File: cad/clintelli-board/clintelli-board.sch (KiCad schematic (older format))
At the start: 26 parts, among them IC1 ATMEGA328-A, P1 CONN_01X16, P2 CONN_01X14, P3 CONN_01X14, P4 CONN_01X01, P5 CONN_01X01, P6 CONN_01X01, SW1 SW_PUSH, U1 3v3, U2 ESP8266EX, U3 ADS1298xPAG, U4 ATECC608A-MAHDA, Y1 16M

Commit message: Schematic changes: - Replaced ESP8266 with ESP32 - Added AudioJack connector - Removed Header pins
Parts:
- removed P1: CONN_01X16, Pin_Headers:Pin_Header_Straight_1x16_Pitch2.54mm, symbol clintelli-board-rescue:CONN_01X16-Pyramiduino-rescue
- removed P2: CONN_01X14, Pin_Headers:Pin_Header_Straight_1x15_Pitch2.54mm, symbol clintelli-board-rescue:CONN_01X15-Pyramiduino-rescue
- removed P3: CONN_01X14, Pin_Headers:Pin_Header_Straight_1x14_Pitch2.54mm, symbol clintelli-board-rescue:CONN_01X14-Pyramiduino-rescue
- removed U2: ESP8266EX, Package_DFN_QFN:QFN-32-1EP_5x5mm_P0.5mm_EP3.45x3.45mm, symbol MCU_Espressif:ESP8266EX
- added J1: AudioJack3_Ground, symbol Connector:AudioJack3_Ground
- added U2: ESP32-WROOM-32, RF_Module:ESP32-WROOM-32, symbol RF_Module:ESP32-WROOM-32
- C1, C2, C3, C4, C5, C6, C7, C8, C9: symbol clintelli-board-rescue:C-Pyramiduino-rescue -> clintelli-board-rescue:C
- D1: symbol clintelli-board-rescue:LED-Pyramiduino-rescue -> clintelli-board-rescue:LED
- IC1: symbol clintelli-board-rescue:ATMEGA328-A-Pyramiduino-rescue -> clintelli-board-rescue:ATMEGA328-A
- L1: symbol clintelli-board-rescue:INDUCTOR-Pyramiduino-rescue -> clintelli-board-rescue:INDUCTOR
- P4, P5, P6: symbol clintelli-board-rescue:CONN_01X01-Pyramiduino-rescue -> clintelli-board-rescue:CONN_01X01
- R1, R2: symbol clintelli-board-rescue:R-Pyramiduino-rescue -> clintelli-board-rescue:R
- SW1: symbol clintelli-board-rescue:SW_PUSH-Pyramiduino-rescue -> clintelli-board-rescue:SW_PUSH
- U1: symbol clintelli-board-rescue:MIC5504-3.3YM5-Pyramiduino-rescue -> clintelli-board-rescue:MIC5504-3.3YM5
- Y1: symbol clintelli-board-rescue:Crystal_GND24-Pyramiduino-rescue -> clintelli-board-rescue:Crystal_GND24
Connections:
- net labels removed: CTS
- wire segments 112 -> 69
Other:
- moved on the sheet: U3, U4

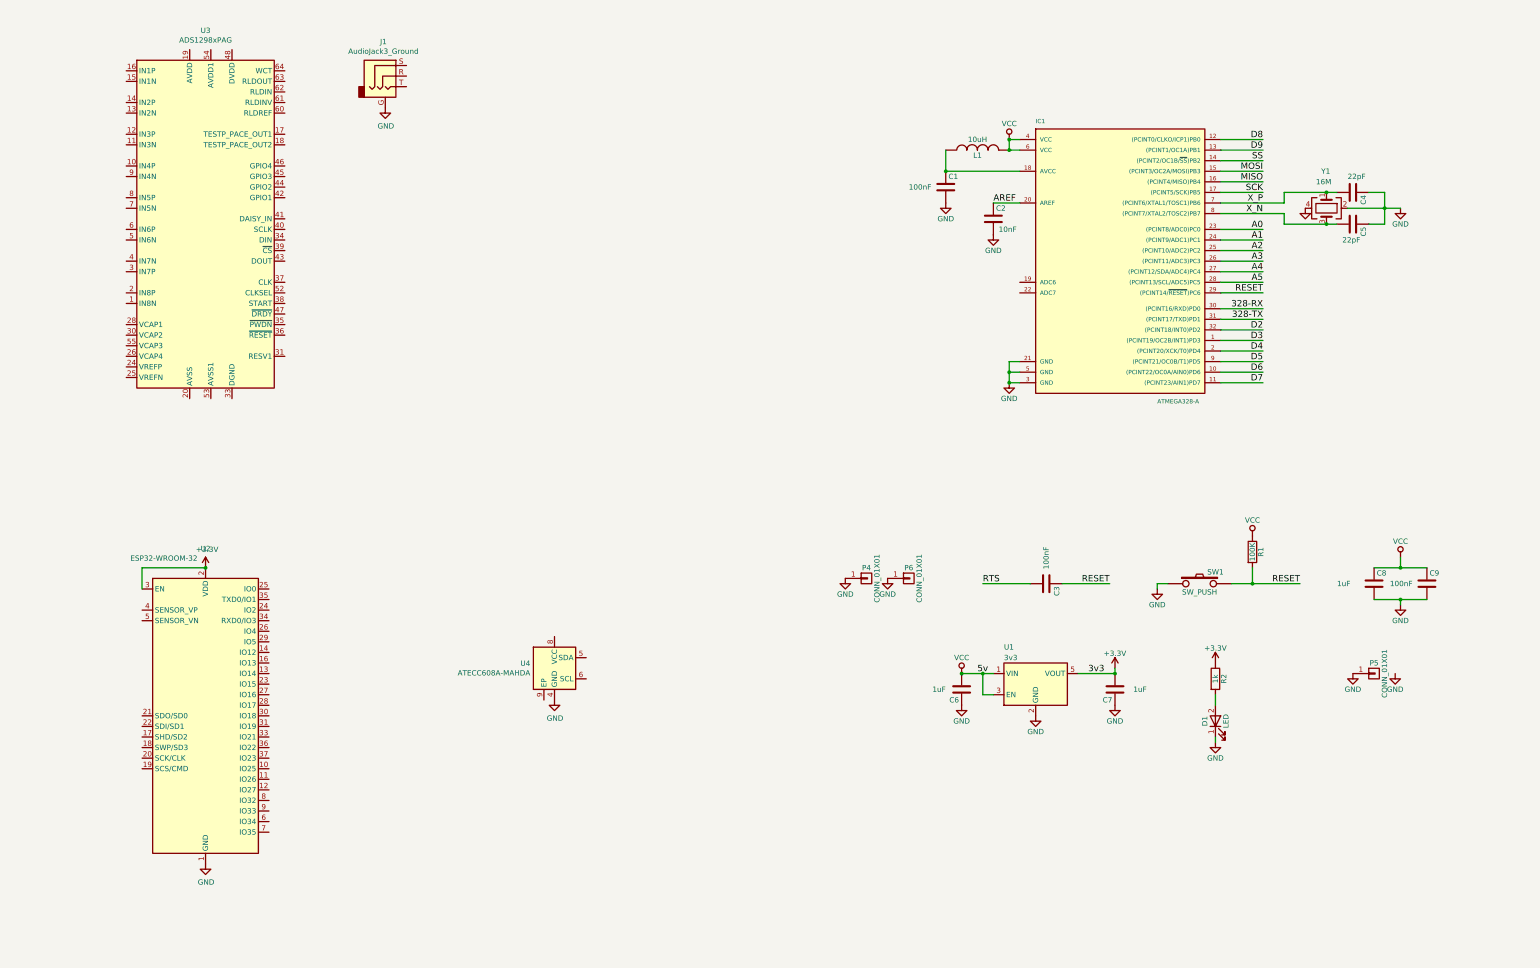
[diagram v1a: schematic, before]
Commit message: Schematic changes: - Annotations - Cortex M4 wiring - Connected ECG with MCU via SPI - Connected 1 ECG Lead
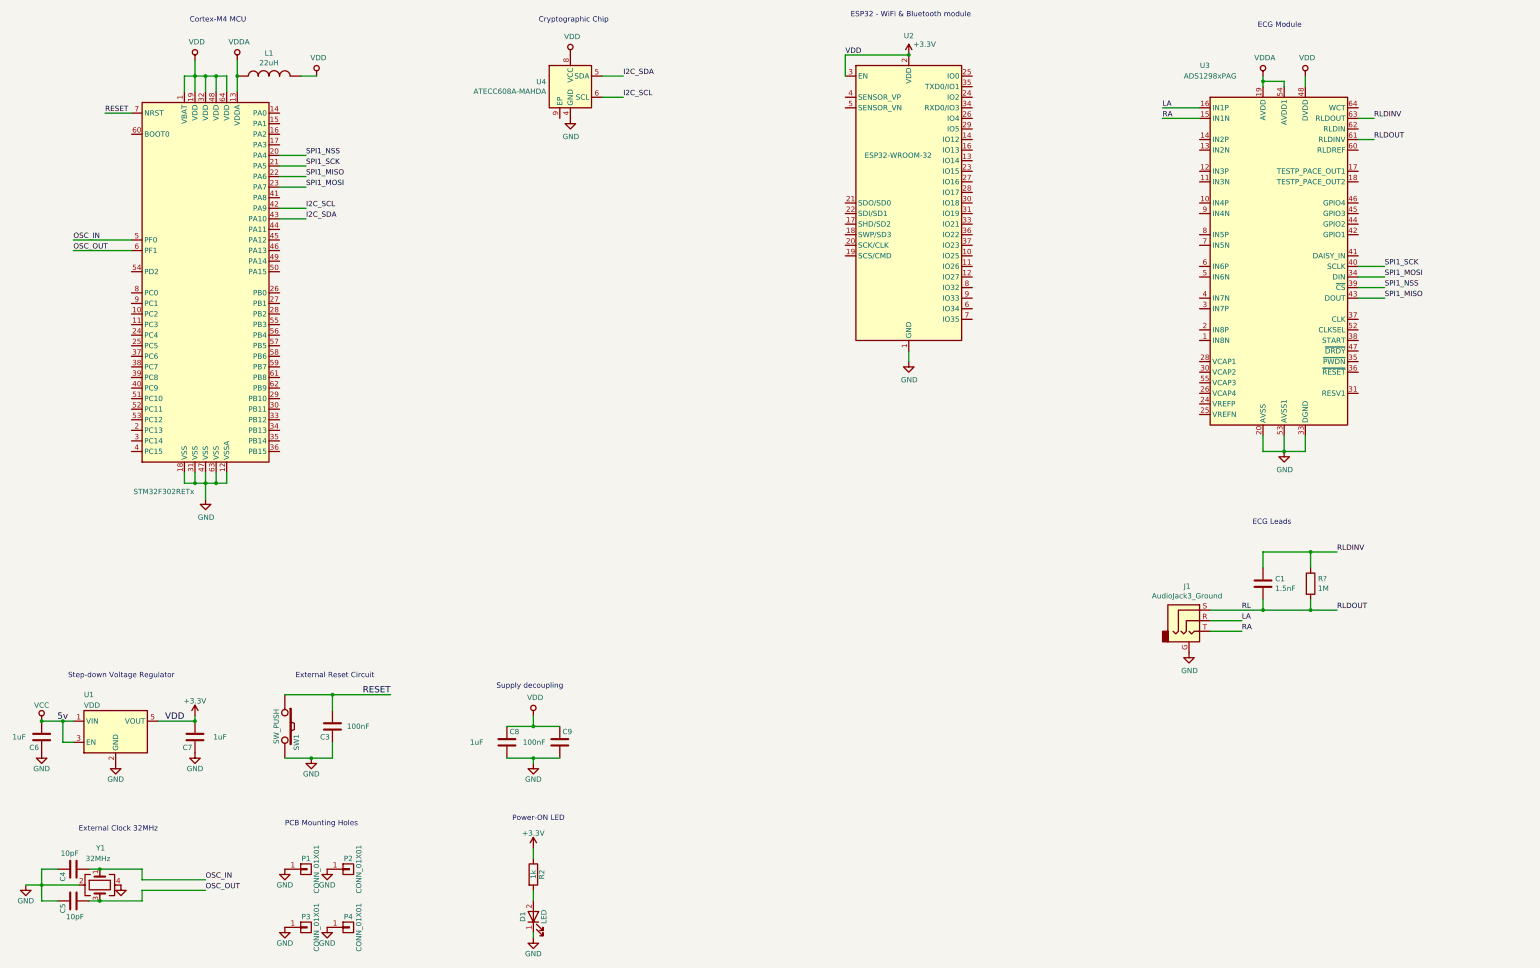
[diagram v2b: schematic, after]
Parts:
- removed C2: 10nF, Capacitors_SMD:C_0805, symbol clintelli-board-rescue:C
- removed IC1: ATMEGA328-A, Housings_DFN_QFN:QFN-32-1EP_5x5mm_Pitch0.5mm, symbol clintelli-board-rescue:ATMEGA328-A
- removed R1: 100K, Capacitors_SMD:C_0805, symbol clintelli-board-rescue:R
- added P4: CONN_01X01, Mounting_Holes:MountingHole_2.2mm_M2_Pad, symbol clintelli-board-rescue:CONN_01X01
- added R?: 1M, symbol clintelli-board-rescue:R
- added U?: STM32F302RETx, Package_QFP:LQFP-64_10x10mm_P0.5mm, symbol MCU_ST_STM32F3:STM32F302RETx
- C1: value 100nF -> 1.5nF; footprint Capacitors_SMD:C_0805 -> (none)
- C4, C5: value 22pF -> 10pF
- L1: value 10uH -> 22uH; footprint Capacitors_SMD:C_0805 -> (none); MFN LQM21FN100N00L -> (none)
- U1: value 3v3 -> VDD
- Y1: value 16M -> 32MHz
- renumbered P4 to P1, P6 to P2, P5 to P3
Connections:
- net RTS is gone; now on net RESET: C3.2
- net +3V3: now also C8.1, C9.1, L1.2, U3.48 (DVDD), U3.50 (DVDD), U4.8 (VCC), U?.1 (VBAT), U?.19 (VDD), U?.32 (VDD), U?.48 (VDD), U?.64 (VDD)
- net GND: now also C3.1, SW1.2, U3.20 (AVSS), U3.23 (AVSS), U3.32 (AVSS), U3.33 (DGND), U3.49 (DGND), U3.51 (DGND), U3.53 (AVSS1), U3.57 (AVSS), U3.58 (AVSS), P4.1 (P1), U?.12 (VSSA), U?.18 (VSS), U?.31 (VSS), U?.47 (VSS), U?.63 (VSS); no longer C1.2, SW1.1
- net RESET: now also SW1.1, U?.7 (NRST); no longer C3.1, SW1.2
- net VCC: no longer C8.1, C9.1, L1.2
- net RLDINV: now reaches C1.1
- net RLDINV: now also U3.63 (RLDOUT), R?.1; no longer L1.1
- net I2C_SDA: now reaches U4.5 (SDA)
- net I2C_SDA: now also U?.43 (PA10)
- net I2C_SCL: now reaches U4.6 (SCL)
- net I2C_SCL: now also U?.42 (PA9)
- net RA: now reaches U3.15 (IN1N)
- net RA: now also J1.T
- net LA: now reaches U3.16 (IN1P)
- net LA: now also J1.R
- net VDDA: now reaches U3.19 (AVDD), U3.21 (AVDD), U3.22 (AVDD), U3.56 (AVDD), U3.59 (AVDD)
- net VDDA: now also L1.1, U3.54 (AVDD1), U?.13 (VDDA)
- net SPI1_MOSI: now reaches U3.34 (DIN)
- net SPI1_MOSI: now also U?.23 (PA7)
- net SPI1_NSS: now reaches U3.39 (~CS)
- net SPI1_NSS: now also U?.20 (PA4)
- net SPI1_SCK: now reaches U3.40 (SCLK)
- net SPI1_SCK: now also U?.21 (PA5)
- net SPI1_MISO: now reaches U3.43 (DOUT)
- net SPI1_MISO: now also U?.22 (PA6)
- net RL: now reaches U3.61 (RLDINV)
- net RL: now also C1.2, J1.S, R?.2
- net X_N renamed OSC_OUT
- net OSC_OUT: now also U?.6 (PF1)
- net X_P renamed OSC_IN
- net OSC_IN: now also U?.5 (PF0)
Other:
- note added: "Cortex-M4 MCU"
- note added: "Cryptographic Chip"
- note added: "ECG Leads"
- note added: "ECG Module"
- note added: "ESP32 - WiFi & Bluetooth module"
- note added: "External Clock 32MHz"
- note added: "External Reset Circuit"
- note added: "PCB Mounting Holes"
- note added: "Power-ON LED"
- note added: "Step-down Voltage Regulator"
- note added: "Supply decoupling"
- moved on the sheet: C3, C4, C5, C6, C7, C8, C9, D1, J1, P1, P2, P3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

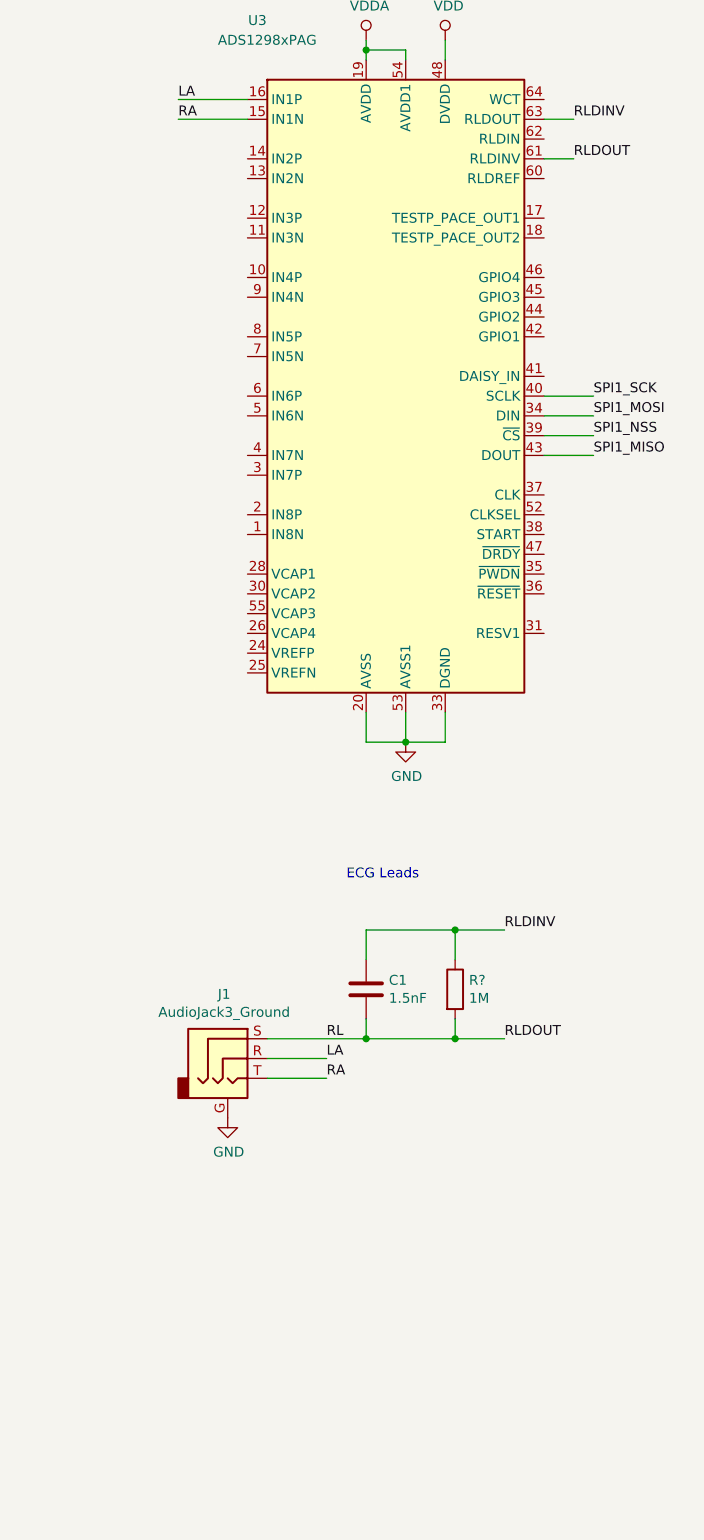
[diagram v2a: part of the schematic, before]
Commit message: Schematic changes: - 12 ECG Leads connectors
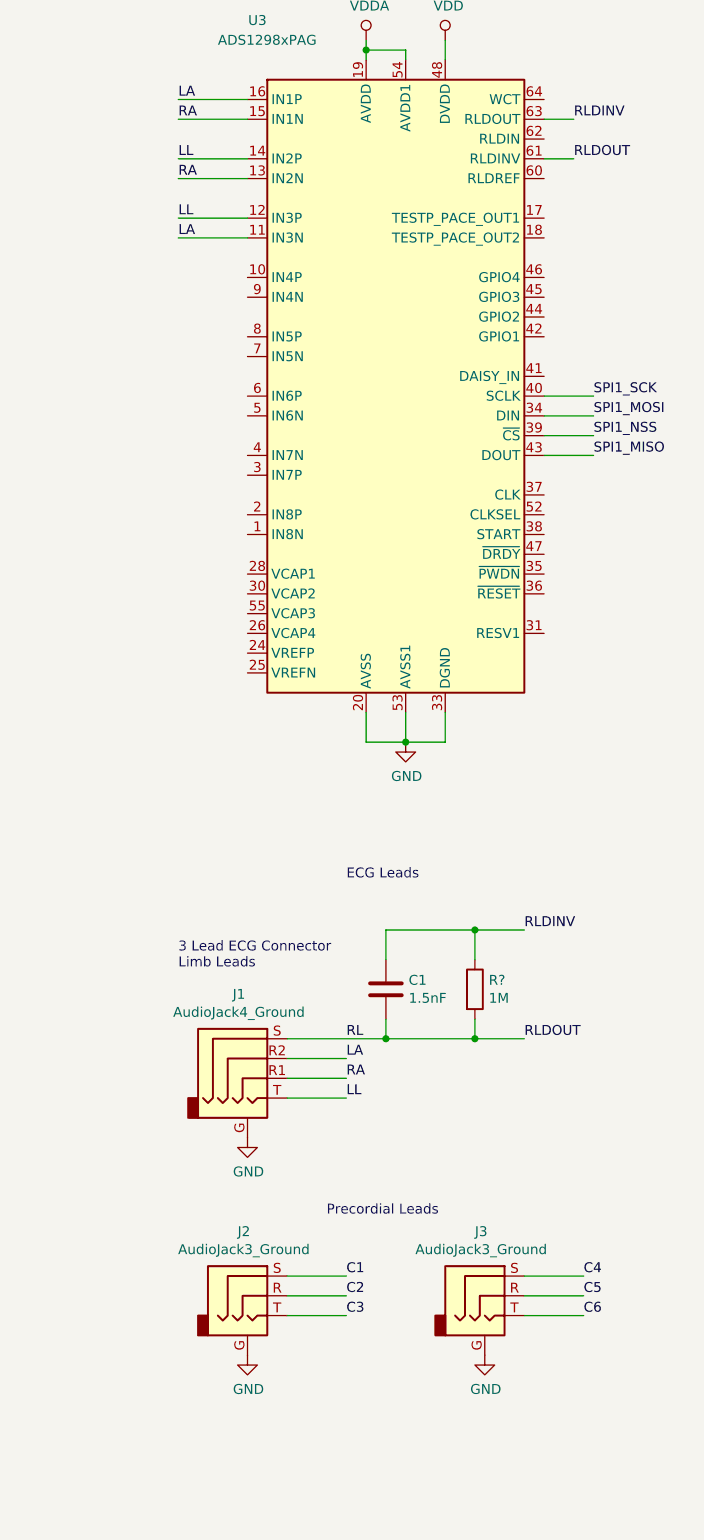
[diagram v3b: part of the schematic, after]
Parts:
- removed J1: AudioJack3_Ground, symbol Connector:AudioJack3_Ground
- added J1: AudioJack4_Ground, symbol Connector:AudioJack4_Ground
- added J2, J3: AudioJack3_Ground, symbol Connector:AudioJack3_Ground
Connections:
- net GND: now also J1.G, J2.G, J3.G
- net LA: now also U3.11 (IN3N), J1.R2
- net RA: now also U3.13 (IN2N), J1.R1
- net RL: now also J1.S
- net LL: now reaches U3.12 (IN3P)
- net LL: now also U3.14 (IN2P), J1.T
- new net C1: J2.S
- new net C2: J2.R
- new net C3: J2.T
- new net C4: J3.S
- new net C5: J3.R
- new net C6: J3.T
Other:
- note added: "3 Lead ECG Connector\nLimb Leads"
- note added: "Precordial Leads"
- moved on the sheet: C1, R?
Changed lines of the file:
@@
-	1    0    0    -1
-$EndComp
-$Comp
-L Connector:AudioJack3_Ground J1
-U 1 1 5D3E13D8
-P 12700 6900
-F 0 "J1" H 12682 7225 50  0000 C CNN
-F 1 "AudioJack3_Ground" H 12682 7134 50  0000 C CNN
-F 2 "" H 12700 6900 50  0001 C CNN
-F 3 "~" H 12700 6900 50  0001 C CNN
-	1    12700 6900
-	1    0    0    -1
-$EndComp
-$Comp
-L power:GND #PWR0104
-U 1 1 5D418A5A
-P 12700 7200
-F 0 "#PWR0104" H 12700 6950 50  0001 C CNN
-F 1 "GND" H 12705 7027 50  0000 C CNN
-F 2 "" H 12700 7200 50  0001 C CNN
-F 3 "" H 12700 7200 50  0001 C CNN
-	1    12700 7200
 	1    0    0    -1
 $EndComp
@@
 SPI1_NSS
 Wire Wire Line
-	12900 6900 13200 6900
-Wire Wire Line
-	12900 7000 13200 7000
-Text Label 13200 6800 0    50   ~ 0
+	13000 6900 13300 6900
+Wire Wire Line
+	13000 7000 13300 7000
+Text Label 13300 6800 0    50   ~ 0
 RL
-Text Label 13200 6900 0    50   ~ 0
+Text Label 13300 6900 0    50   ~ 0
 LA
-Text Label 13200 7000 0    50   ~ 0
+Text Label 13300 7000 0    50   ~ 0
 RA
 Wire Wire Line
@@
 RA
 Wire Wire Line
-	13400 6800 13400 6700
-Wire Wire Line
-	12900 6800 13400 6800
+	13500 6800 13500 6700
+Wire Wire Line
+	13000 6800 13500 6800
 $Comp
 L clintelli-board-rescue:C C1
 U 1 1 5D39BEC5
-P 13400 6550
-F 0 "C1" H 13515 6596 50  0000 L CNN
-F 1 "1.5nF" H 13515 6505 50  0000 L CNN
-F 2 "" H 13438 6400 50  0001 C CNN
-F 3 "" H 13400 6550 50  0001 C CNN
-	1    13400 6550
-	1    0    0    -1
-$EndComp
-Wire Wire Line
-	13400 6800 13850 6800
-Wire Wire Line
-	13850 6800 13850 6700
-Connection ~ 13400 6800
+P 13500 6550
+F 0 "C1" H 13615 6596 50  0000 L CNN
+F 1 "1.5nF" H 13615 6505 50  0000 L CNN
+F 2 "" H 13538 6400 50  0001 C CNN
+F 3 "" H 13500 6550 50  0001 C CNN
+	1    13500 6550
+	1    0    0    -1
+$EndComp
+Wire Wire Line
+	13500 6800 13950 6800
+Wire Wire Line
+	13950 6800 13950 6700
+Connection ~ 13500 6800
 $Comp
 L clintelli-board-rescue:R R?
 U 1 1 5D3B5D43
-P 13850 6550
-F 0 "R?" H 13920 6596 50  0000 L CNN
-F 1 "1M" H 13920 6505 50  0000 L CNN
-F 2 "" V 13780 6550 50  0001 C CNN
-F 3 "" H 13850 6550 50  0001 C CNN
-	1    13850 6550
-	1    0    0    -1
-$EndComp
-Wire Wire Line
-	13850 6800 14100 6800
-Connection ~ 13850 6800
-Wire Wire Line
-	13400 6400 13400 6250
-Wire Wire Line
-	13400 6250 13850 6250
-Wire Wire Line
-	13850 6400 13850 6250
-Connection ~ 13850 6250
-Wire Wire Line
-	13850 6250 14100 6250
+P 13950 6550
+F 0 "R?" H 14020 6596 50  0000 L CNN
+F 1 "1M" H 14020 6505 50  0000 L CNN
+F 2 "" V 13880 6550 50  0001 C CNN
+F 3 "" H 13950 6550 50  0001 C CNN
+	1    13950 6550
+	1    0    0    -1
+$EndComp
+Wire Wire Line
+	13950 6800 14200 6800
+Connection ~ 13950 6800
+Wire Wire Line
+	13500 6400 13500 6250
+Wire Wire Line
+	13500 6250 13950 6250
+Wire Wire Line
+	13950 6400 13950 6250
+Connection ~ 13950 6250
+Wire Wire Line
+	13950 6250 14200 6250
 Wire Wire Line
 	14300 2150 14450 2150
@@
 Text Label 14450 2350 0    50   ~ 0
 RLDOUT
-Text Label 14100 6250 0    50   ~ 0
+Text Label 14200 6250 0    50   ~ 0
 RLDINV
-Text Label 14100 6800 0    50   ~ 0
+Text Label 14200 6800 0    50   ~ 0
 RLDOUT
 Text Notes 13300 6000 0    50   ~ 0
 ECG Leads
+$Comp
+L Connector:AudioJack4_Ground J1
+U 1 1 5D4233CD
+P 12800 6900
+F 0 "J1" H 12757 7225 50  0000 C CNN
+F 1 "AudioJack4_Ground" H 12757 7134 50  0000 C CNN
+F 2 "" H 12800 6900 50  0001 C CNN
+F 3 "~" H 12800 6900 50  0001 C CNN
+	1    12800 6900
+	1    0    0    -1
+$EndComp
+$Comp
+L power:GND #PWR0104
+U 1 1 5D418A5A
+P 12800 7300
+F 0 "#PWR0104" H 12800 7050 50  0001 C CNN
+F 1 "GND" H 12805 7127 50  0000 C CNN
+F 2 "" H 12800 7300 50  0001 C CNN
+F 3 "" H 12800 7300 50  0001 C CNN
+	1    12800 7300
+	1    0    0    -1
+$EndComp
+Wire Wire Line
+	13000 7100 13300 7100
+Text Label 13300 7100 0    50   ~ 0
+LL
+Text Notes 12450 6450 0    50   ~ 0
+3 Lead ECG Connector\nLimb Leads
+Wire Wire Line
+	12800 2350 12450 2350
+Wire Wire Line
+	12800 2450 12450 2450
+Wire Wire Line
+	12800 2650 12450 2650
+Wire Wire Line
+	12800 2750 12450 2750
+Text Label 12450 2350 0    50   ~ 0
+LL
+Text Label 12450 2450 0    50   ~ 0
+RA
+Text Label 12450 2650 0    50   ~ 0
+LL
+Text Label 12450 2750 0    50   ~ 0
+LA
+$Comp
+L Connector:AudioJack3_Ground J2
+U 1 1 5D455865
+P 12800 8100
+F 0 "J2" H 12782 8425 50  0000 C CNN
+F 1 "AudioJack3_Ground" H 12782 8334 50  0000 C CNN
+F 2 "" H 12800 8100 50  0001 C CNN
+F 3 "~" H 12800 8100 50  0001 C CNN
+	1    12800 8100
+	1    0    0    -1
+$EndComp
+$Comp
+L Connector:AudioJack3_Ground J3
+U 1 1 5D455FF1
+P 14000 8100
+F 0 "J3" H 13982 8425 50  0000 C CNN
+F 1 "AudioJack3_Ground" H 13982 8334 50  0000 C CNN
+F 2 "" H 14000 8100 50  0001 C CNN
+F 3 "~" H 14000 8100 50  0001 C CNN
+	1    14000 8100
+	1    0    0    -1
+$EndComp
+Wire Wire Line
+	13000 8000 13300 8000
+Wire Wire Line
+	13000 8100 13300 8100
+Wire Wire Line
+	13000 8200 13300 8200
+Wire Wire Line
+	14200 8000 14500 8000
+Wire Wire Line
+	14200 8100 14500 8100
+Wire Wire Line
+	14200 8200 14500 8200
+Text Label 13300 8000 0    50   ~ 0
+C1
+Text Label 13300 8100 0    50   ~ 0
+C2
+Text Label 13300 8200 0    50   ~ 0
+C3
+Text Label 14500 8000 0    50   ~ 0
+C4
+Text Label 14500 8100 0    50   ~ 0
+C5
+Text Label 14500 8200 0    50   ~ 0
+C6
+$Comp
+L clintelli-board-rescue:GND #PWR?
+U 1 1 5D469CCB
+P 12800 8400
+F 0 "#PWR?" H 12800 8150 50  0001 C CNN
+F 1 "GND" H 12805 8227 50  0000 C CNN
+F 2 "" H 12800 8400 50  0001 C CNN
+F 3 "" H 12800 8400 50  0001 C CNN
+	1    12800 8400
+	1    0    0    -1
+$EndComp
+$Comp
+L clintelli-board-rescue:GND #PWR?
+U 1 1 5D46A059
+P 14000 8400
+F 0 "#PWR?" H 14000 8150 50  0001 C CNN
+F 1 "GND" H 14005 8227 50  0000 C CNN
+F 2 "" H 14000 8400 50  0001 C CNN
+F 3 "" H 14000 8400 50  0001 C CNN
+	1    14000 8400
+	1    0    0    -1
+$EndComp
+Text Notes 13200 7700 0    50   ~ 0
+Precordial Leads
 $EndSCHEMATC
